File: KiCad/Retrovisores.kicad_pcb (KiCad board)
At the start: 2 copper layers, 66 parts, among them J1 Conn_01x02_Pin, J10 Conn_01x07_Pin, J11 Conn_01x02_Pin, J2 DE9_Pins, J3 Conn_01x04_Pin, J4 DE9_Pins, J5 Conn_01x02_Pin, J6 Conn_01x02_Pin, J7 Conn_01x02_Pin, J8 Conn_PIC_ICSP_ICD, J9 Conn_01x04_Pin, K2 Relay_SPDT, Q14 AO3400A, Q15 AO3401A, Q16 AO3400A, Q17 AO3401A, Q18 AO3400A, Q19 AO3401A, Q20 AO3400A, Q21 AO3401A, Q22 AO3400A, Q23 AO3401A, Q24 AO3400A, Q25 AO3401A, Q27 AO3400A, SW1 SW_Push, SW2 SW_Push, SW3 SW_Push, SW4 SW_Push, SW6 SW_Nidec_CAS-120A1, U2 SN65HVD232, U4 LT1117-3.3, U5 TSR3-2450N, U7 PIC32MX250F128D-IPT, Y1 Crystal

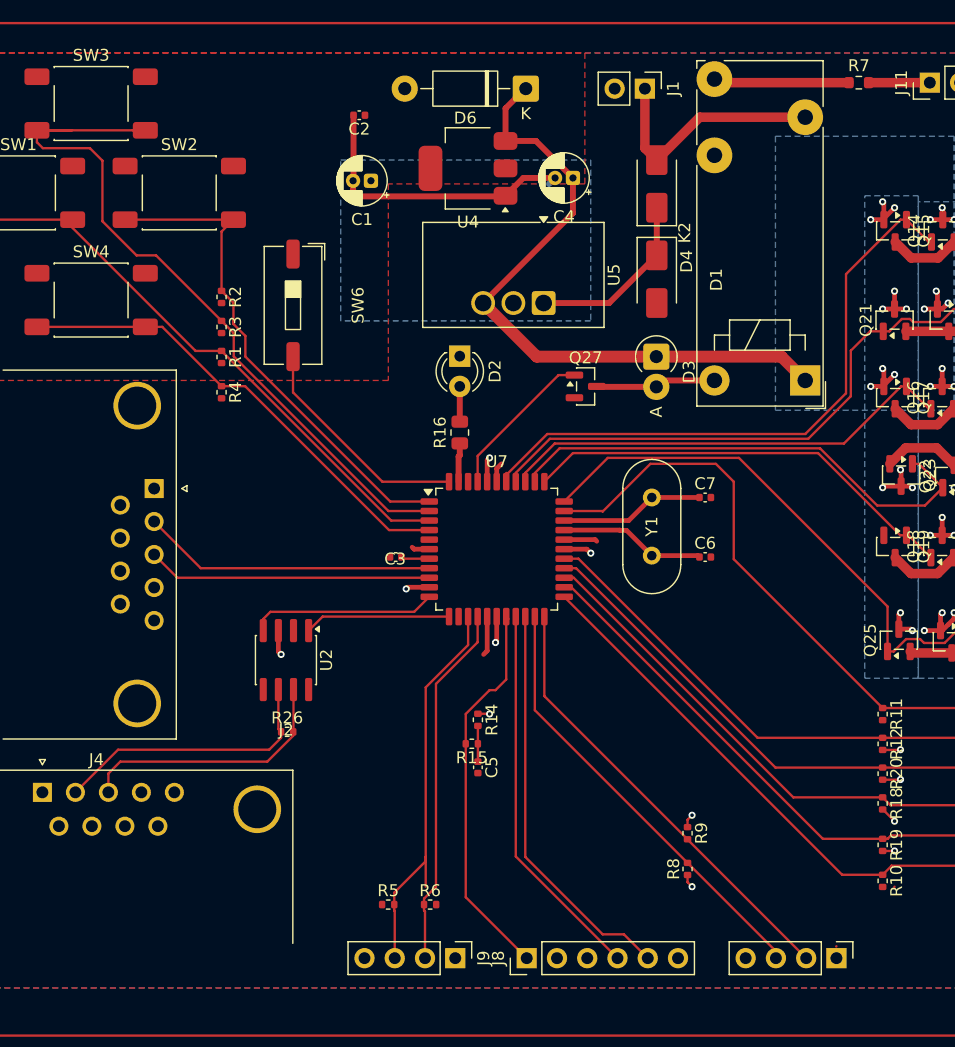
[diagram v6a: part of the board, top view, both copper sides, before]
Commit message: he corretgit un error en l'asignasio de pins del micro el qu eha fet que el routing y el placement canviin una mica
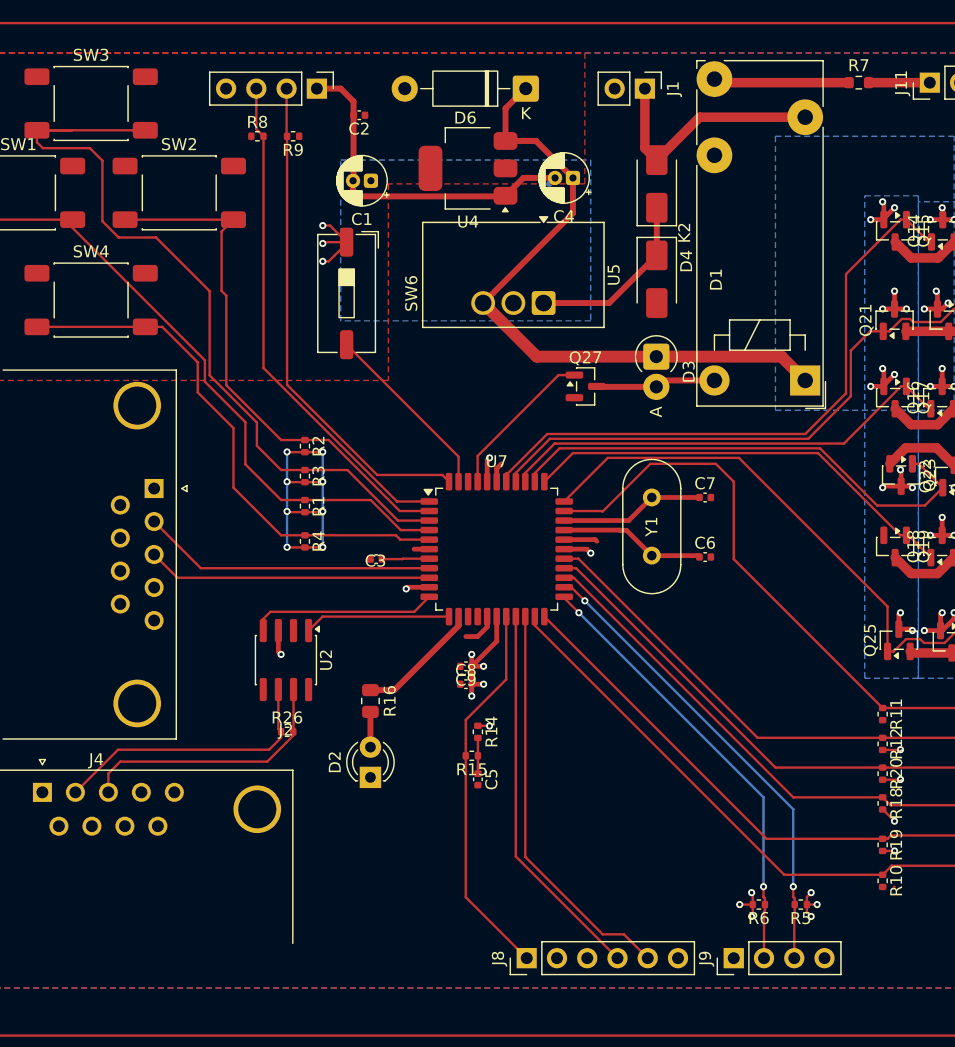
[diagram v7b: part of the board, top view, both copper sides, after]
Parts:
- added C8: 100n, Capacitor_SMD:C_0402_1005Metric, F.Cu at (132.0, 80.5)
- added C9: 100n, Capacitor_SMD:C_0402_1005Metric, F.Cu at (132.0, 79.0)
- moved J3 85.0 mm to (119.5, 30.5)
- moved R8 71.3 mm to (114.5, 34.5), turned to 0 degrees
- moved R9 67.2 mm to (117.5, 34.5), turned to 180 degrees
- moved D2 36.2 mm to (124.0, 88.3), turned to 90 degrees
- moved R5 34.6 mm to (160.1, 99.0), turned to 180 degrees
- moved R6 27.6 mm to (156.6, 99.0), turned to 180 degrees
- moved R16 23.8 mm to (124.0, 81.9), turned to -90 degrees
- moved J9 23.4 mm to (154.5, 103.5), turned to 90 degrees
- moved R3 14.3 mm to (118.5, 63.0)
- moved R4 14.3 mm to (118.5, 68.5)
- moved R1 14.3 mm to (118.5, 65.5)
- moved R2 14.3 mm to (118.5, 60.5)
- moved SW6 4.61 mm to (122.0, 47.7)
- moved C3 1.65 mm to (124.5, 70.0)
- moved R14 1.01 mm to (133.0, 84.5)
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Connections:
- D2 pad 1: unconnected-(D2-K-Pad1) -> GND
- R16 pad 1: Net-(U7-RB7) -> Net-(U7-RA7)
- U7 pad 1: L -> DI2C
- U7 pad 13: unconnected-(U7-RA7-Pad13) -> Net-(U7-RA7)
- U7 pad 14: SCL -> unconnected-(U7-RB14-Pad14)
- U7 pad 15: SDA -> unconnected-(U7-RB15-Pad15)
- U7 pad 2: U -> L
- U7 pad 21: DI2C -> FC6
- U7 pad 22: KLKI2C -> FC5
- U7 pad 23: FC6 -> SDA
- U7 pad 24: FC5 -> SCL
- U7 pad 3: R -> U
- U7 pad 4: D -> R
- U7 pad 43: Net-(U7-RB7) -> OP//CL
- U7 pad 44: OP//CL -> KLKI2C
- U7 pad 5: unconnected-(U7-RC9-Pad5) -> D
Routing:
- net GND: track 57.8 -> 90.0 mm, vias 18 -> 26
- net VCC: track 14.1 -> 35.0 mm, vias 8 -> 18
- net Net-(U7-RA7): track 0.00 -> 10.4 mm
- net SDA: track 30.6 -> 37.4 mm, vias 0 -> 2
- net SCL: track 33.8 -> 39.5 mm, vias 0 -> 2
- net DI2C: track 37.1 -> 42.3 mm
- net D: track 40.0 -> 44.7 mm
- net U: track 64.0 -> 68.5 mm
- net KLKI2C: track 37.8 -> 41.9 mm
- net Net-(U7-RB7): track 3.82 -> 0.00 mm
- net OP//CL: track 19.2 -> 15.4 mm
- net R: track 49.9 -> 53.4 mm
- net L: track 42.4 -> 45.0 mm
- net FC6: track 47.7 -> 49.9 mm
- net Net-(U7-VCAP): track 2.20 -> 3.99 mm
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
